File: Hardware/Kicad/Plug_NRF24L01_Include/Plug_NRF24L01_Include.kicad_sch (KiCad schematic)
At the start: 54 parts, among them J1 Conn_01x07_Socket, J2 Conn_02x07_Odd_Even, Q1 2N7002, Q2 2N7002, Q3 2N7002, Q4 2N7002, Q5 2N7002, SW2 SW_SPST, U1 STM32L412KBTx, U2 MIC5219-3.3YMM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

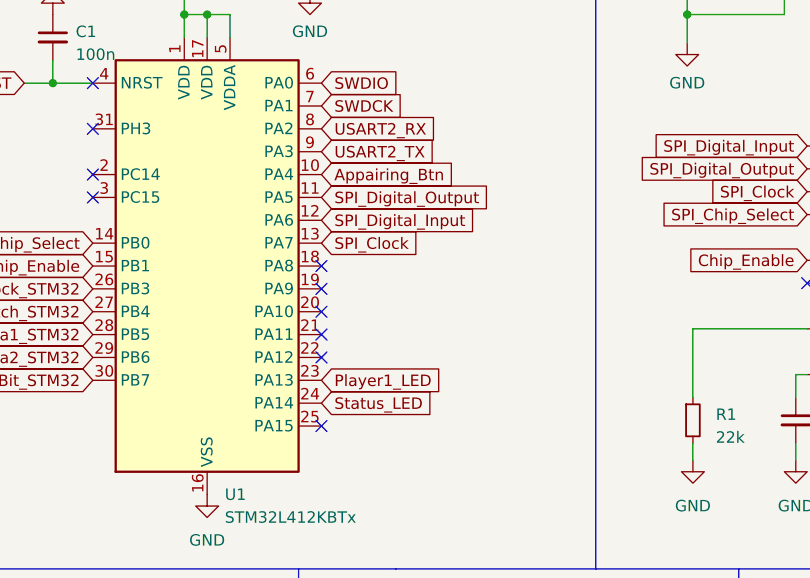
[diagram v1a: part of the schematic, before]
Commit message: Updated Plug_NRF24L01_Include (V1.1) - PCB
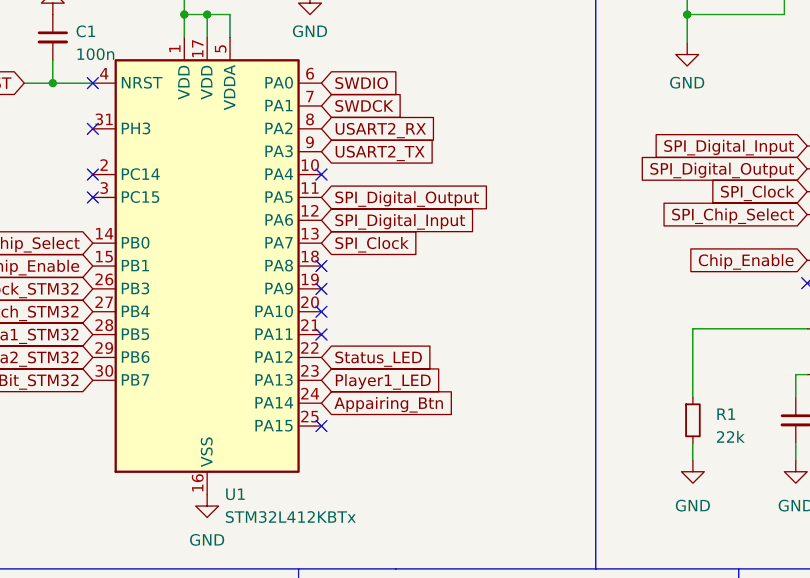
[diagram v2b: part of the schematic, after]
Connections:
- net Appairing_Btn: now also U1.24 (PA14); no longer U1.10 (PA4)
- net Status_LED: now also U1.22 (PA12); no longer U1.24 (PA14)
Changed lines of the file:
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@@
   (no_connect (at 76.835 127.635))
   (no_connect (at 35.56 55.88))
+  (no_connect (at 60.96 53.34))
   (no_connect (at 60.96 66.04))
   (no_connect (at 76.835 122.555))
@@
   (no_connect (at 89.535 112.395))
   (no_connect (at 60.96 63.5))
-  (no_connect (at 60.96 73.66))
   (no_connect (at 35.56 43.18))
   (wire (pts (xy 101.6 35.56) (xy 101.6 33.655))
@@
     )
   )
+  (global_label "Appairing_Btn" (shape input) (at 60.96 78.74 0) (fields_autoplaced)
+    (effects (font (size 1.27 1.27)) (justify left))
+    (property "Intersheetrefs" "${INTERSHEET_REFS}" (at 76.8075 78.74 0)
+      (effects (font (size 1.27 1.27)) (justify left) hide)
+    )
+  )
   (global_label "ANT2" (shape input) (at 119.38 107.95 180) (fields_autoplaced)
     (effects (font (size 1.27 1.27)) (justify right))
@@
     )
   )
-  (global_label "Status_LED" (shape input) (at 60.96 78.74 0) (fields_autoplaced)
-    (effects (font (size 1.27 1.27)) (justify left))
-    (property "Intersheetrefs" "${INTERSHEET_REFS}" (at 74.2675 78.74 0)
-      (effects (font (size 1.27 1.27)) (justify left) hide)
-    )
-  )
   (global_label "ANT2" (shape input) (at 145.415 60.325 0) (fields_autoplaced)
     (effects (font (size 1.27 1.27)) (justify left))
@@
     )
   )
-  (global_label "Appairing_Btn" (shape input) (at 60.96 53.34 0) (fields_autoplaced)
-    (effects (font (size 1.27 1.27)) (justify left))
-    (property "Intersheetrefs" "${INTERSHEET_REFS}" (at 76.8075 53.34 0)
-      (effects (font (size 1.27 1.27)) (justify left) hide)
-    )
-  )
   (global_label "Serial_Data1_SNES" (shape input) (at 34.925 120.65 0) (fields_autoplaced)
     (effects (font (size 1.27 1.27)) (justify left))
@@
       (effects (font (size 1.27 1.27)) (justify left) hide)
     )
+  )
+  (global_label "Status_LED" (shape input) (at 60.96 73.66 0) (fields_autoplaced)
+    (effects (font (size 1.27 1.27)) (justify left))
+    (property "Intersheetrefs" "${INTERSHEET_REFS}" (at 74.2675 73.66 0)
+      (effects (font (size 1.27 1.27)) (justify left) hide)
+    )

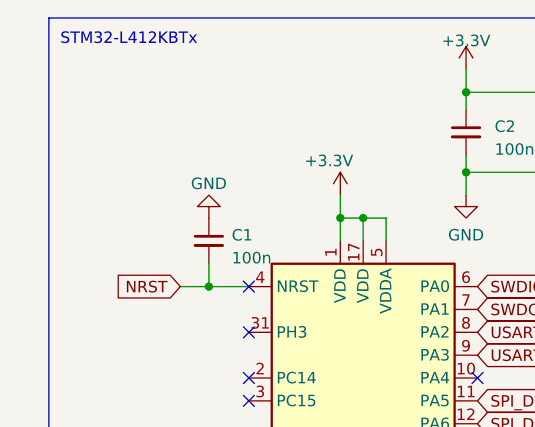
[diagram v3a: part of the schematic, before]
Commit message: Added a capacitor of 10u for the power of the STM32 on the schematics of the plugs
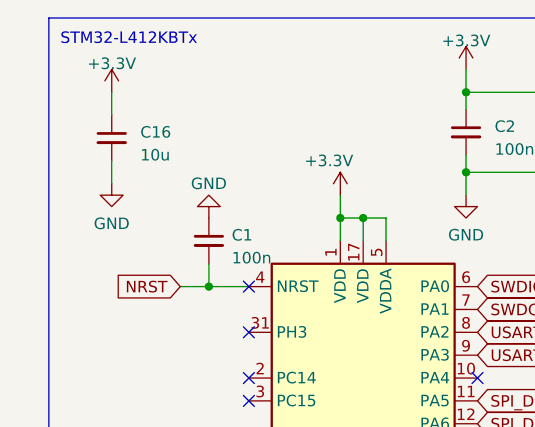
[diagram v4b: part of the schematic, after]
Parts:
- added C16: 10u, Capacitor_SMD:C_0603_1608Metric_Pad1.08x0.95mm_HandSolder, symbol Device:C_Small
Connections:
- net +3.3V: now also C16.1
- net GND: now also C16.2
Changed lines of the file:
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@@
     (stroke (width 0) (type default))
   )
+  (wire (pts (xy 20.32 21.59) (xy 20.32 24.13))
+    (stroke (width 0) (type default))
+  )
   (wire (pts (xy 103.505 157.48) (xy 103.505 160.02))
     (stroke (width 0) (type default))
@@
     (stroke (width 0) (type default))
   )
+  (wire (pts (xy 20.32 29.21) (xy 20.32 31.75))
+    (stroke (width 0) (type default))
+  )
   (wire (pts (xy 48.26 38.1) (xy 48.26 35.56))
     (stroke (width 0) (type default))
@@
     )
   )
+  (symbol (lib_id "power:+3.3V") (at 20.32 21.59 0) (unit 1)
+    (in_bom yes) (on_board yes) (dnp no) (fields_autoplaced)
+    (property "Reference" "#PWR041" (at 20.32 25.4 0)
+      (effects (font (size 1.27 1.27)) hide)
+    )
+    (property "Value" "+3.3V" (at 20.32 18.415 0)
+      (effects (font (size 1.27 1.27)))
+    )
+    (property "Footprint" "" (at 20.32 21.59 0)
+      (effects (font (size 1.27 1.27)) hide)
+    )
+    (property "Datasheet" "" (at 20.32 21.59 0)
+      (effects (font (size 1.27 1.27)) hide)
+    )
+    (pin "1")
+    (instances
+      (project "Plug_NRF24L01_Include"
+        (path "/0058c30e-85d4-47b6-bff0-8d9f01f30c52"
+          (reference "#PWR041") (unit 1)
+        )
+      )
+      (project "Test"
+        (path "/e27c4aed-f26e-4205-8842-b91be8be392b"
+          (reference "#PWR05") (unit 1)
+        )
+      )
+    )
+  )
   (symbol (lib_id "Device:L_Small") (at 132.08 115.57 90) (unit 1)
     (in_bom yes) (on_board yes) (dnp no)
@@
     )
   )
+  (symbol (lib_id "Device:C_Small") (at 20.32 26.67 0) (unit 1)
+    (in_bom yes) (on_board yes) (dnp no)
+    (property "Reference" "C16" (at 23.495 26.035 0)
+      (effects (font (size 1.27 1.27)) (justify left))
+    )
+    (property "Value" "10u" (at 23.495 28.575 0)
+      (effects (font (size 1.27 1.27)) (justify left))
+    )
+    (property "Footprint" "Capacitor_SMD:C_0603_1608Metric_Pad1.08x0.95mm_HandSolder" (at 20.32 26.67 0)
+      (effects (font (size 1.27 1.27)) hide)
+    )
+    (property "Datasheet" "~" (at 20.32 26.67 0)
+      (effects (font (size 1.27 1.27)) hide)
+    )
+    (pin "1")
+    (pin "2")
+    (instances
+      (project "Plug_NRF24L01_Include"
+        (path "/0058c30e-85d4-47b6-bff0-8d9f01f30c52"
+          (reference "C16") (unit 1)
+        )
+      )
+    )
+  )
   (symbol (lib_id "power:GND") (at 128.27 130.175 0) (unit 1)
     (in_bom yes) (on_board yes) (dnp no) (fields_autoplaced)
@@
         )
       )
+    )
+  )
+  (symbol (lib_id "power:GND") (at 20.32 31.75 0) (unit 1)
+    (in_bom yes) (on_board yes) (dnp no) (fields_autoplaced)
+    (property "Reference" "#PWR042" (at 20.32 38.1 0)
+      (effects (font (size 1.27 1.27)) hide)
+    )
+    (property "Value" "GND" (at 20.32 36.195 0)
+      (effects (font (size 1.27 1.27)))
+    )
+    (property "Footprint" "" (at 20.32 31.75 0)
+      (effects (font (size 1.27 1.27)) hide)
+    )
+    (property "Datasheet" "" (at 20.32 31.75 0)
+      (effects (font (size 1.27 1.27)) hide)
+    )
+    (pin "1")
+    (instances
+      (project "Plug_NRF24L01_Include"
+        (path "/0058c30e-85d4-47b6-bff0-8d9f01f30c52"
+          (reference "#PWR042") (unit 1)
+        )
+      )
+      (project "Test"
+        (path "/e27c4aed-f26e-4205-8842-b91be8be392b"
+          (reference "#PWR08") (unit 1)
+        )
+      )
